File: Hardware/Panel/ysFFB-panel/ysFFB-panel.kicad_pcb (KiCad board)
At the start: 2 copper layers, 200 x 200 mm, 26 parts

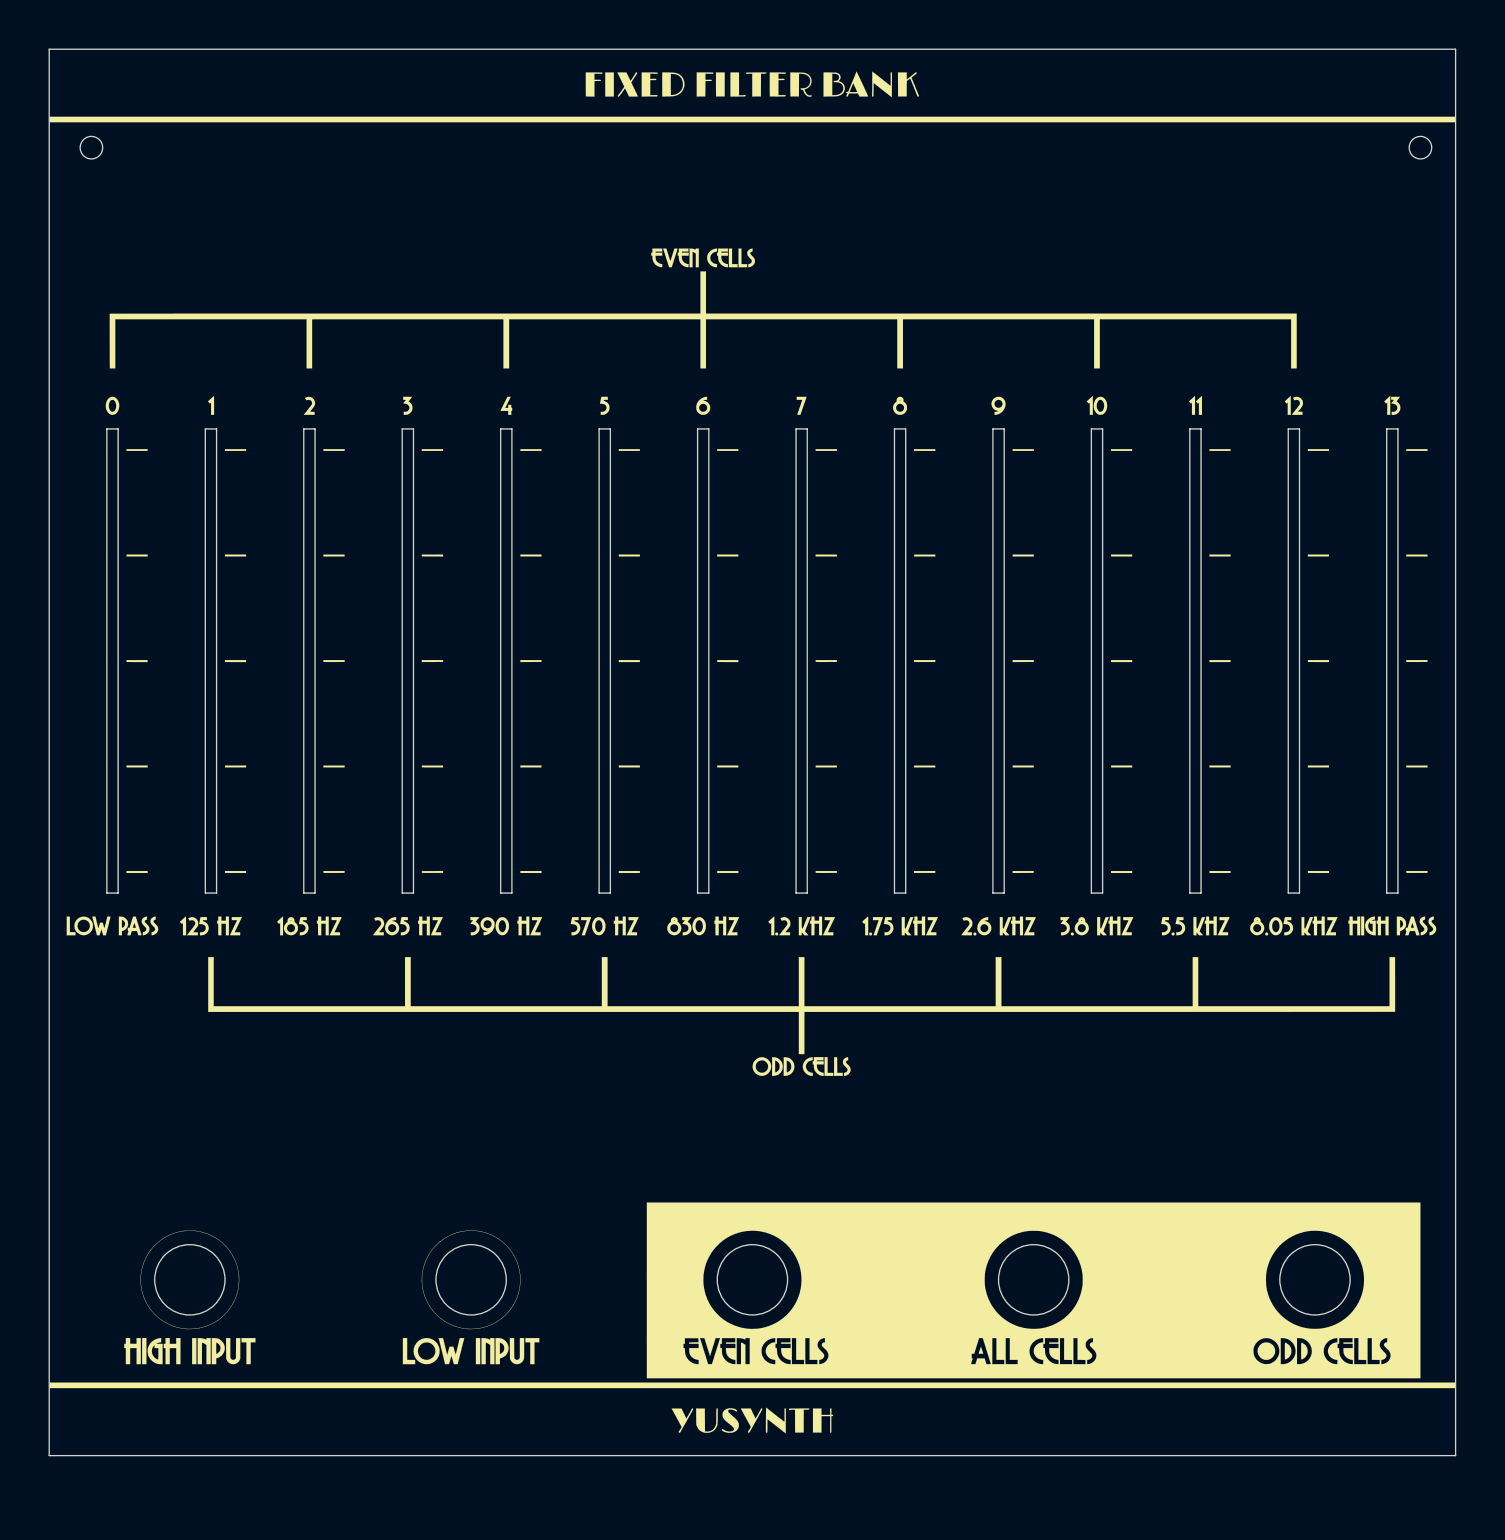
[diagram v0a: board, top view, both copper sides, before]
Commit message: Revised NPTH scheme
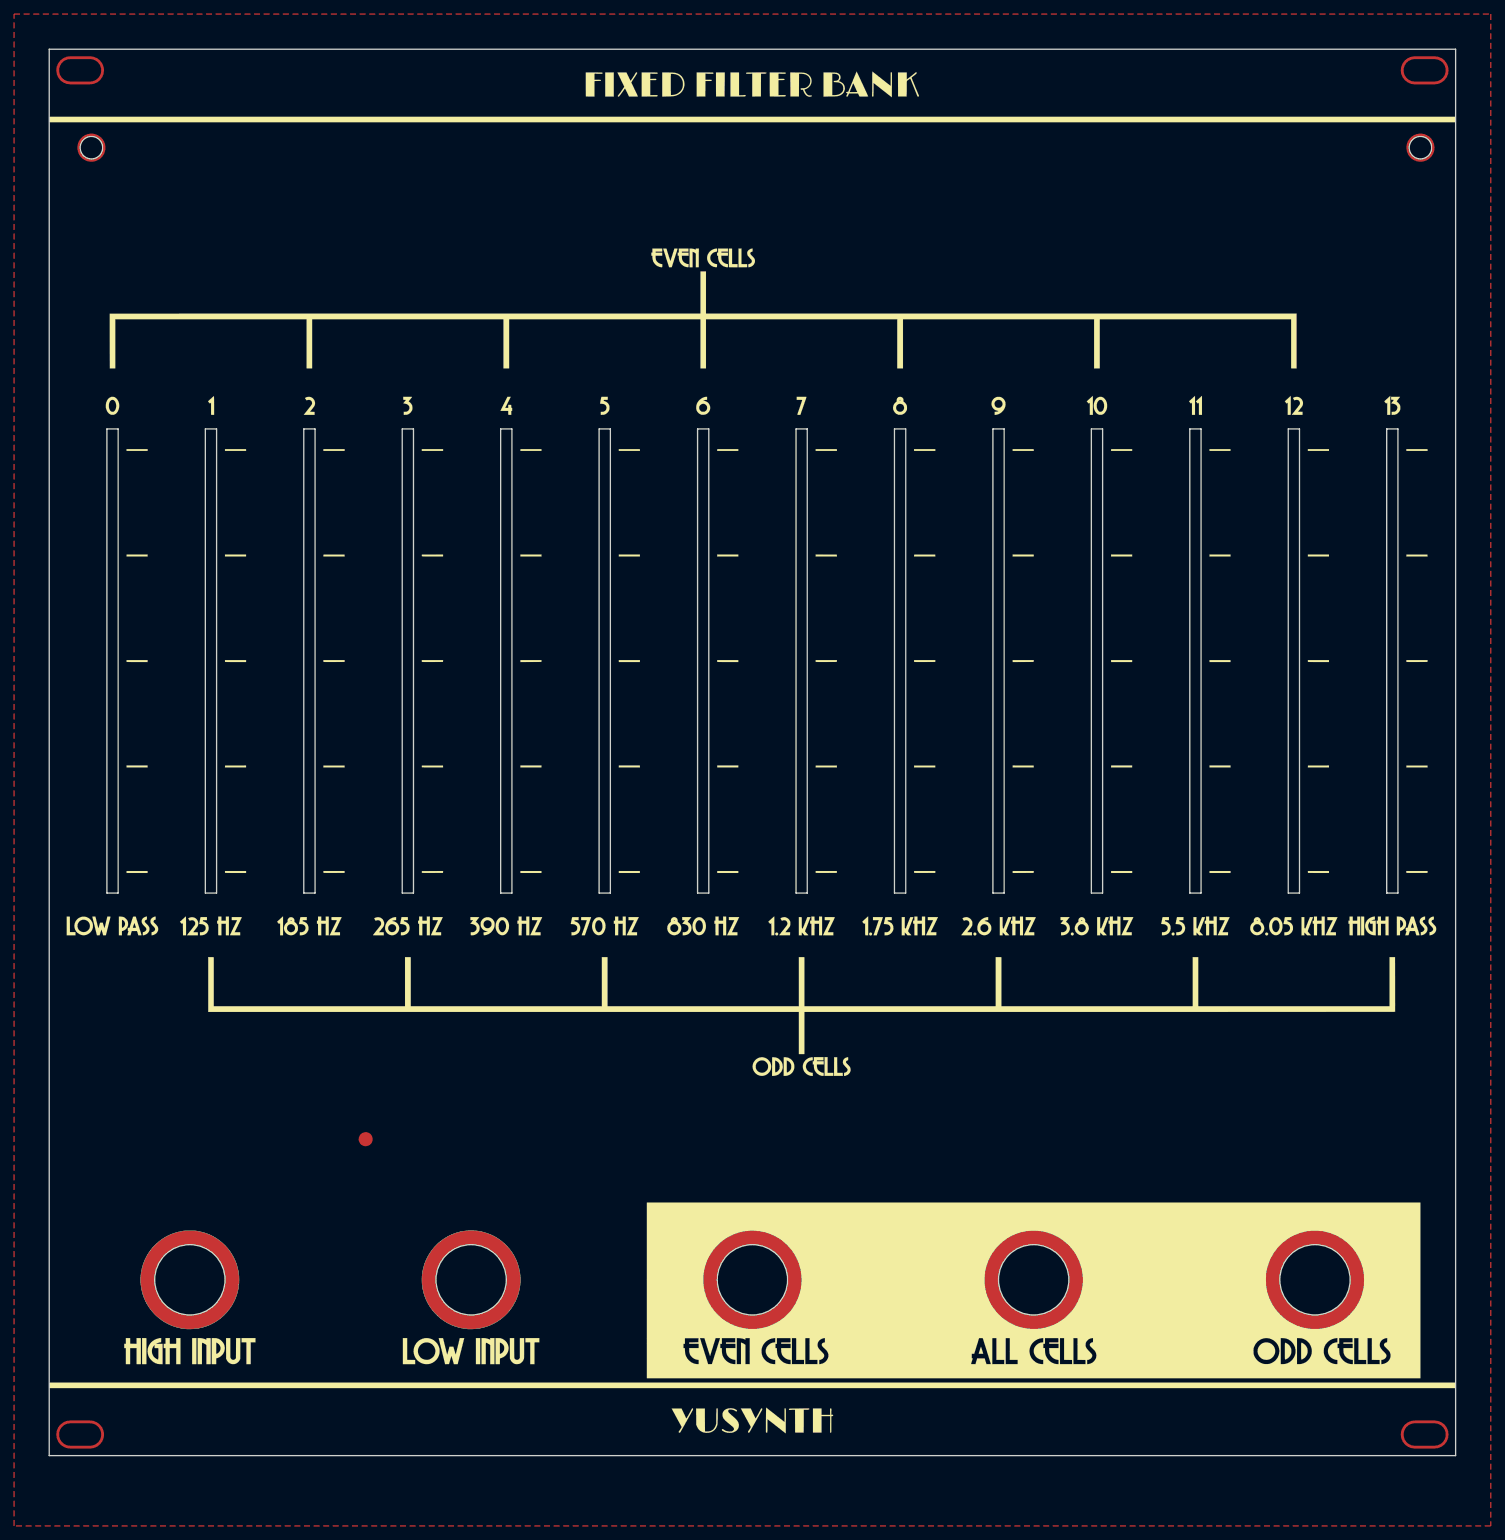
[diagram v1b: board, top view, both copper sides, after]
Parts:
- added GP1: Ground_point_for_NPTH, Kosmo_panel:Ground_point_for_NPTH, F.Cu at (45.0, 155.0)
- H1, H2: footprint Kosmo_panel:Kosmo_Panel_Dual_Slotted_Mounting_Hole_NPTH -> Kosmo_panel:Kosmo_Panel_Dual_Slotted_Mounting_Holes_NPTH
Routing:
- added copper zone on F.Cu, net GND

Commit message: No NPTH specialization
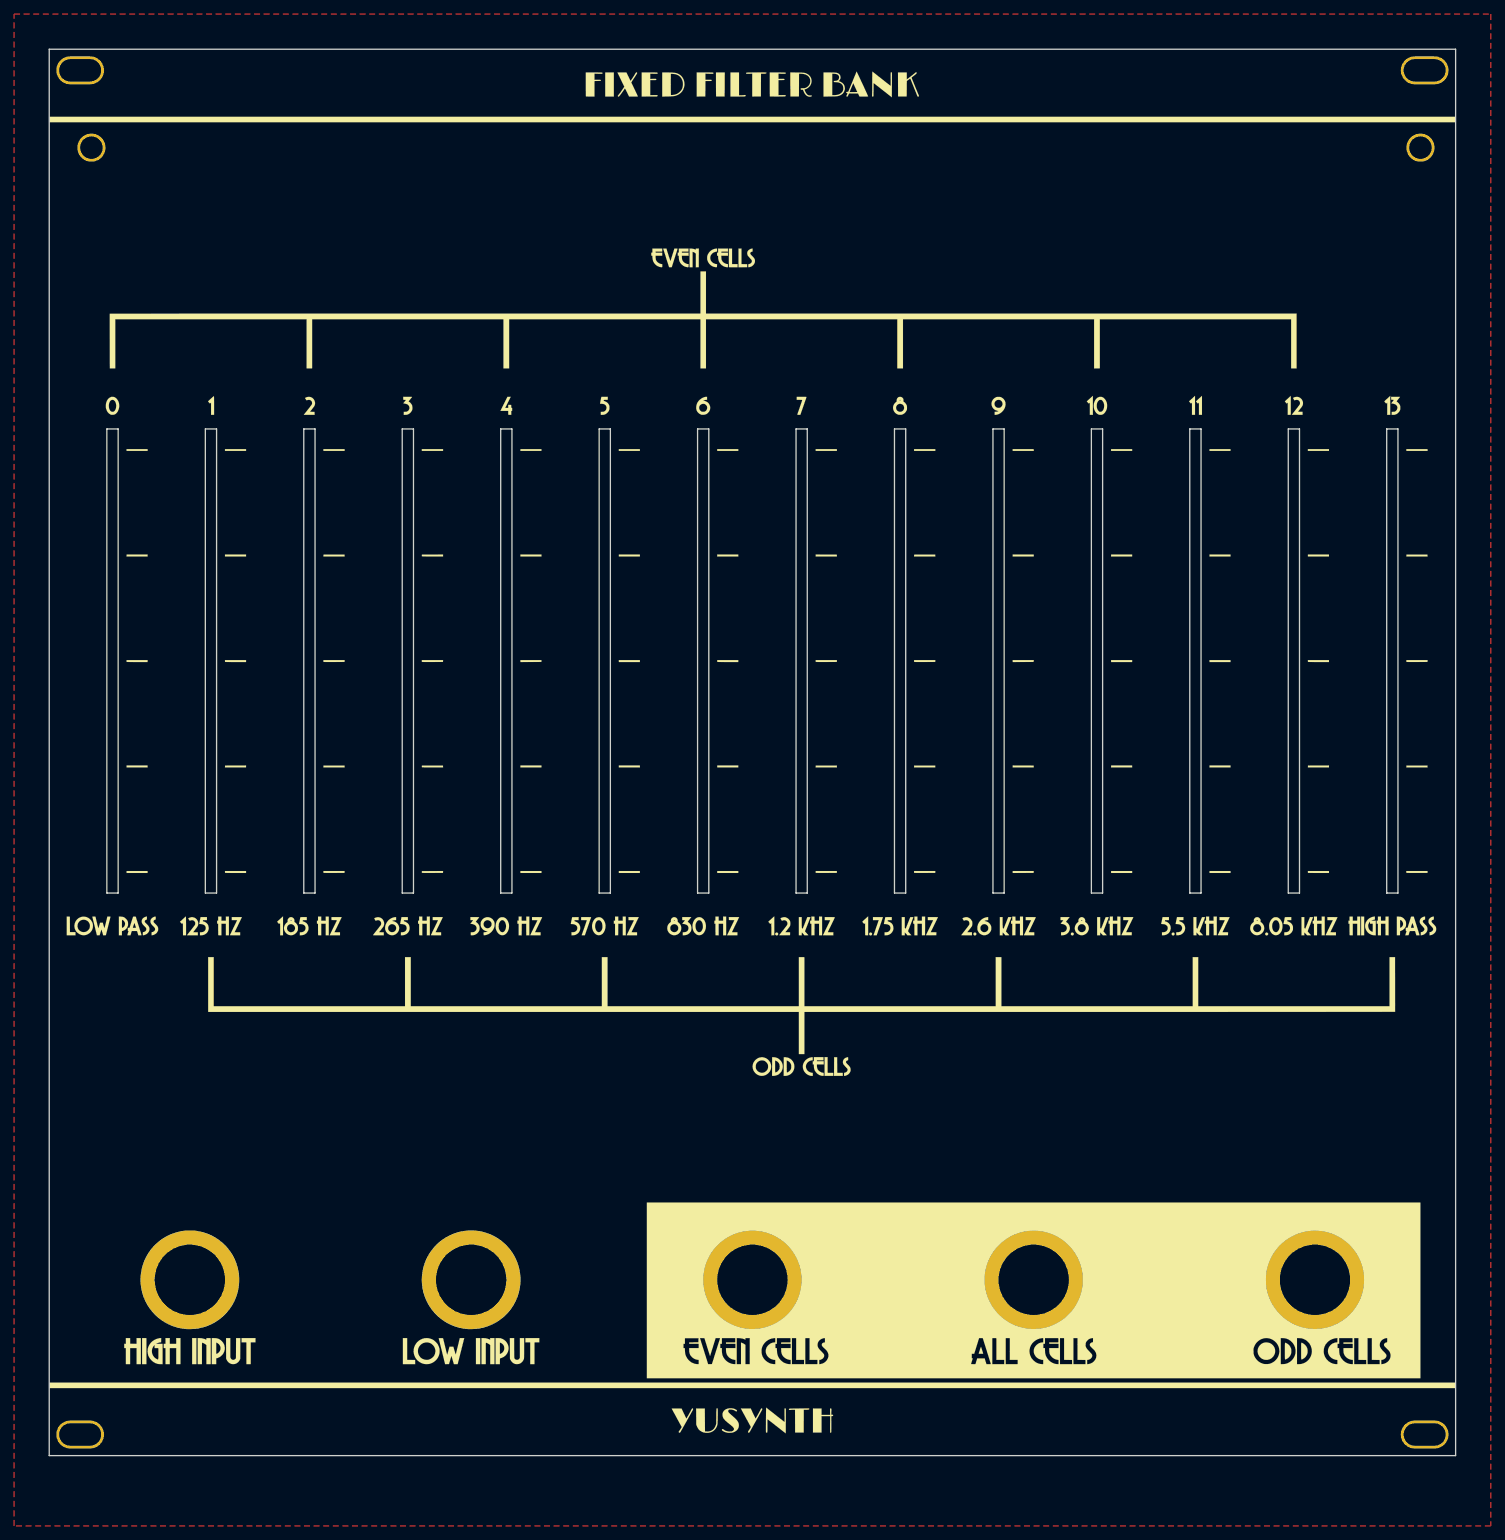
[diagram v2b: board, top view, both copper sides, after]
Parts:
- removed GP1: Ground_point_for_NPTH, Kosmo_panel:Ground_point_for_NPTH
- H1, H2: footprint Kosmo_panel:Kosmo_Panel_Dual_Slotted_Mounting_Holes_NPTH -> Kosmo_panel:Kosmo_Panel_Dual_Slotted_Mounting_Holes
- H10, H13, H16, H19, H5: footprint Kosmo_panel:Kosmo_Jack_Hole_NPTH -> Kosmo_panel:Kosmo_Jack_Hole
- H6, H7: footprint Kosmo_panel:Kosmo_Panel_Mounting_Hole_NPTH -> Kosmo_panel:Kosmo_Panel_Mounting_Hole

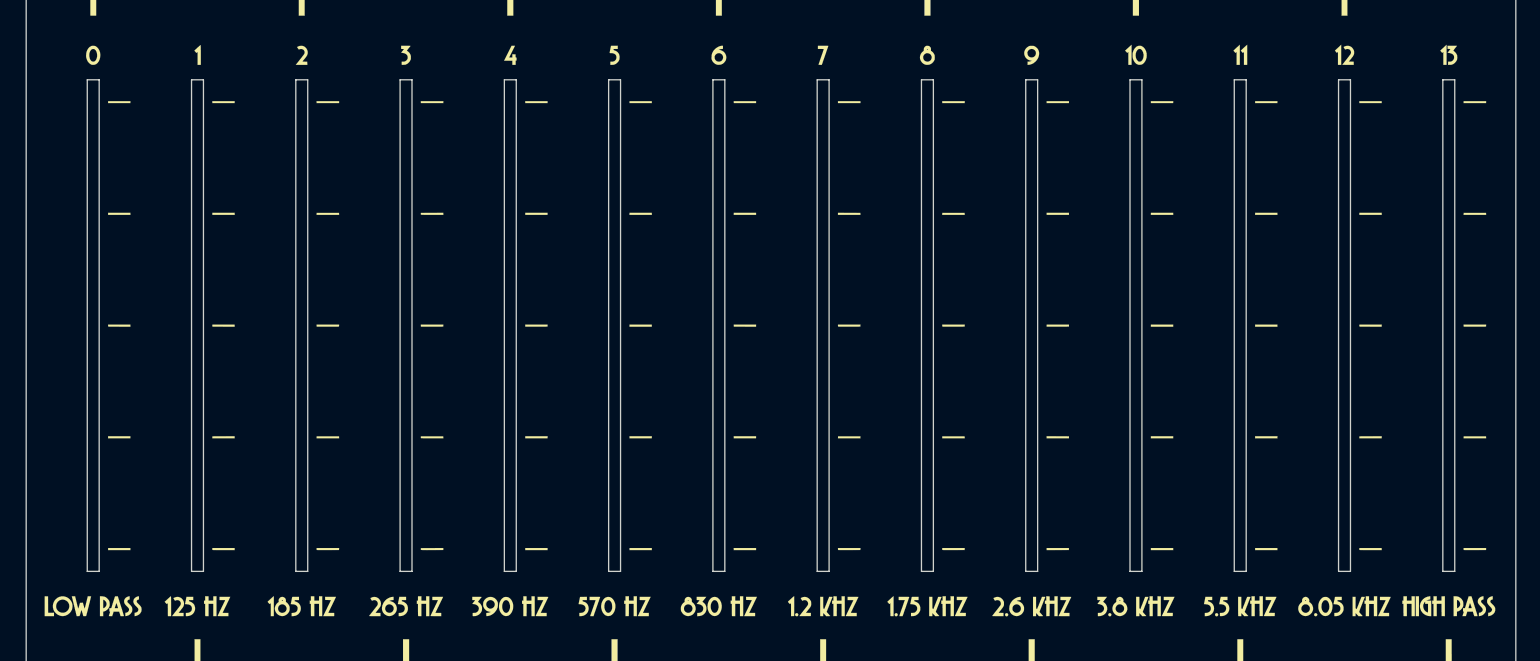
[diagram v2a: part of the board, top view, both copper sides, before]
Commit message: Cap vals on PCB, revised panel
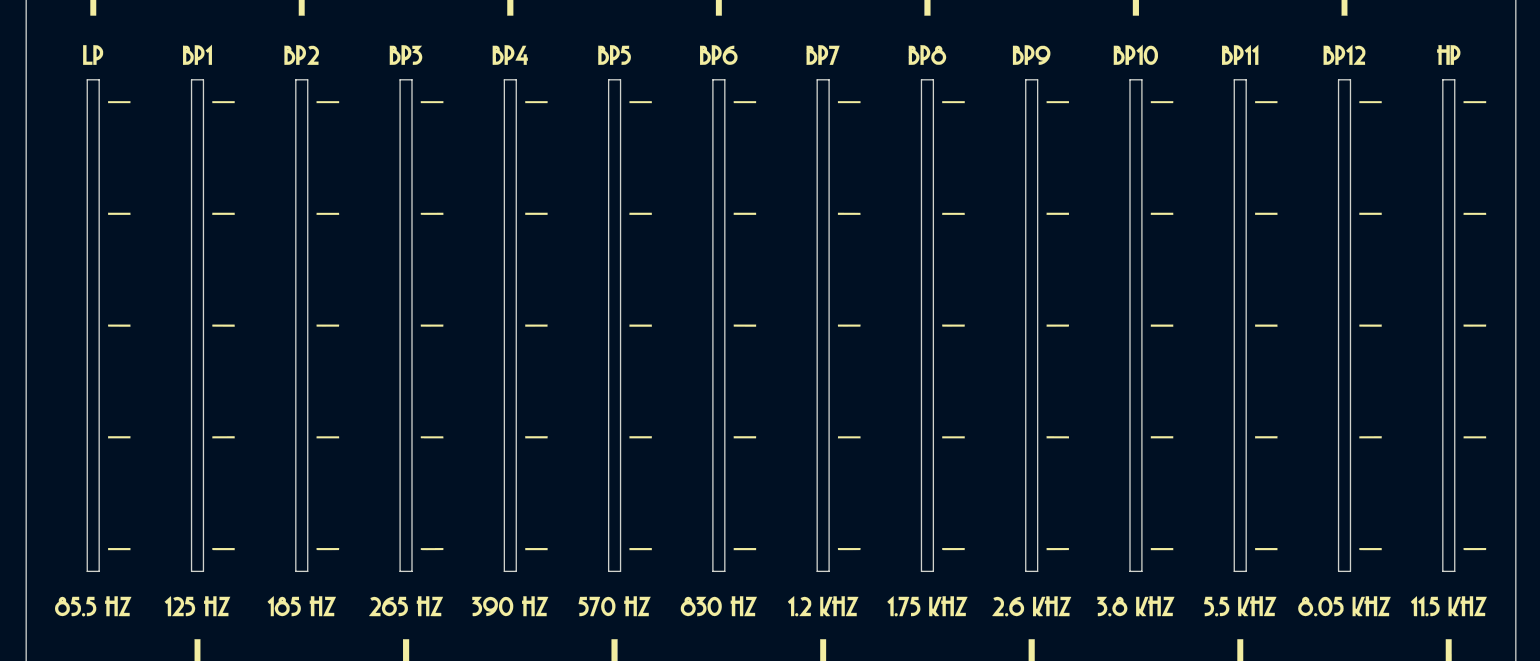
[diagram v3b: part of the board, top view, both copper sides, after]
